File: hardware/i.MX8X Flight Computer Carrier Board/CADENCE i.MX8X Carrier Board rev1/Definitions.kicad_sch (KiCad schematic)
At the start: 12 parts, among them U43 TXS0101DCKR, U44 TXS0101DCKR, U45 TXS0101DCKR, U46 TXS0101DCKR, U47 TXS0108EPW

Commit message: peripheral & connector layout update
- finished rs-422 payload connector layout (changed footprint, package being used has around 40 left in stock at JLCPCB)
- modified memory (mram & nor flash) ic layouts & organized into layout blocks for easy placement later
- revised & reorganized gps, rtc, temp sensor, imu connections into separate layout  blocks. also moved around gps and moved peripherals into completed layout circuit block section for later placement
- changed some power monitor shunt resistor footprints so 10W or so doesnt go thru a sad 0402 resistor lol
- fixed microSD connection issues
- adjusted gps 50 ohm coax impedance connection (28 ohm trace + 22ohm resistor)
- 50 ohm impedance calculations for gps added to schematic & disclaimer for switching regulator low ripple burst mode added to power schematic page

to do:
- verify that board power monitor wont lead to reverse current driving i.mx8x and make it explode
- look further into & verify that cmos image sensor connector is correct one being used by lucid
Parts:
- renumbered R181 to R159, R182 to R160, R183 to R161, R184 to R162, R185 to R163
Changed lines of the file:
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@@
 		(on_board yes)
 		(dnp no)
-		(property "Reference" "R183"
+		(property "Reference" "R161"
 			(at 139.7 24.13 0)
 			(effects
@@
 			(project "CADENCE i.MX8X Carrier Board rev1"
 				(path "/de284495-d382-47cb-b528-76e440980d40/f5f49c98-aaea-4f03-a1b3-a277d1d06600/b523867a-62fb-4a81-ab53-06050067b1aa"
-					(reference "R183")
+					(reference "R161")
 					(unit 1)
 				)
@@
 		(on_board yes)
 		(dnp no)
-		(property "Reference" "R181"
+		(property "Reference" "R159"
 			(at 48.26 44.45 0)
 			(effects
@@
 			(project "CADENCE i.MX8X Carrier Board rev1"
 				(path "/de284495-d382-47cb-b528-76e440980d40/f5f49c98-aaea-4f03-a1b3-a277d1d06600/b523867a-62fb-4a81-ab53-06050067b1aa"
-					(reference "R181")
+					(reference "R159")
 					(unit 1)
 				)
@@
 		(on_board yes)
 		(dnp no)
-		(property "Reference" "R182"
+		(property "Reference" "R160"
 			(at 49.53 22.86 0)
 			(effects
@@
 			(project "CADENCE i.MX8X Carrier Board rev1"
 				(path "/de284495-d382-47cb-b528-76e440980d40/f5f49c98-aaea-4f03-a1b3-a277d1d06600/b523867a-62fb-4a81-ab53-06050067b1aa"
-					(reference "R182")
+					(reference "R160")
 					(unit 1)
 				)
@@
 		(dnp no)
 		(fields_autoplaced yes)
-		(property "Reference" "#FLG034"
+		(property "Reference" "#FLG032"
 			(at 209.55 24.765 0)
 			(effects
@@
 			(project "CADENCE i.MX8X Carrier Board rev1"
 				(path "/de284495-d382-47cb-b528-76e440980d40/f5f49c98-aaea-4f03-a1b3-a277d1d06600/b523867a-62fb-4a81-ab53-06050067b1aa"
-					(reference "#FLG034")
+					(reference "#FLG032")
 					(unit 1)
 				)
@@
 		(on_board yes)
 		(dnp no)
-		(property "Reference" "R185"
+		(property "Reference" "R163"
 			(at 222.25 26.67 0)
 			(effects
@@
 			(project "CADENCE i.MX8X Carrier Board rev1"
 				(path "/de284495-d382-47cb-b528-76e440980d40/f5f49c98-aaea-4f03-a1b3-a277d1d06600/b523867a-62fb-4a81-ab53-06050067b1aa"
-					(reference "R185")
+					(reference "R163")
 					(unit 1)
 				)
@@
 		(on_board yes)
 		(dnp no)
-		(property "Reference" "R184"
+		(property "Reference" "R162"
 			(at 139.7 45.72 0)
 			(effects
@@
 			(project "CADENCE i.MX8X Carrier Board rev1"
 				(path "/de284495-d382-47cb-b528-76e440980d40/f5f49c98-aaea-4f03-a1b3-a277d1d06600/b523867a-62fb-4a81-ab53-06050067b1aa"
-					(reference "R184")
+					(reference "R162")
 					(unit 1)
 				)
@@
 		(dnp no)
 		(fields_autoplaced yes)
-		(property "Reference" "#FLG033"
+		(property "Reference" "#FLG031"
 			(at 83.185 30.48 0)
 			(effects
@@
 			(project "CADENCE i.MX8X Carrier Board rev1"
 				(path "/de284495-d382-47cb-b528-76e440980d40/f5f49c98-aaea-4f03-a1b3-a277d1d06600/b523867a-62fb-4a81-ab53-06050067b1aa"
-					(reference "#FLG033")
-					(unit 1)
-				)
+					(reference "#FLG031")
+					(unit 1)
+				)

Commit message: layout update
- removed vbus regulators (left vbus unconnected for now, will reconnect to vbus on som later)
- outbound signal connectors to adcs & ebyte placement with i2c buffers and power monitors, etc
- layout block placement and some connections
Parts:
- renumbered C144 to C140, C145 to C141, U43 to U41, U44 to U42, U45 to U43, U46 to U44, U47 to U45
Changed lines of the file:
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@@
 		(on_board yes)
 		(dnp no)
-		(property "Reference" "#PWR0274"
+		(property "Reference" "#PWR0269"
 			(at 237.49 26.67 0)
 			(effects
@@
 			(project "CADENCE i.MX8X Carrier Board rev1"
 				(path "/de284495-d382-47cb-b528-76e440980d40/f5f49c98-aaea-4f03-a1b3-a277d1d06600/b523867a-62fb-4a81-ab53-06050067b1aa"
-					(reference "#PWR0274")
+					(reference "#PWR0269")
 					(unit 1)
 				)
@@
 		(on_board yes)
 		(dnp no)
-		(property "Reference" "#PWR0264"
+		(property "Reference" "#PWR0259"
 			(at 80.01 52.07 0)
 			(effects
@@
 			(project "CADENCE i.MX8X Carrier Board rev1"
 				(path "/de284495-d382-47cb-b528-76e440980d40/f5f49c98-aaea-4f03-a1b3-a277d1d06600/b523867a-62fb-4a81-ab53-06050067b1aa"
-					(reference "#PWR0264")
+					(reference "#PWR0259")
 					(unit 1)
 				)
@@
 		(on_board yes)
 		(dnp no)
-		(property "Reference" "#PWR0271"
+		(property "Reference" "#PWR0266"
 			(at 171.45 53.34 0)
 			(effects
@@
 			(project "CADENCE i.MX8X Carrier Board rev1"
 				(path "/de284495-d382-47cb-b528-76e440980d40/f5f49c98-aaea-4f03-a1b3-a277d1d06600/b523867a-62fb-4a81-ab53-06050067b1aa"
-					(reference "#PWR0271")
+					(reference "#PWR0266")
 					(unit 1)
 				)
@@
 		(on_board yes)
 		(dnp no)
-		(property "Reference" "U45"
+		(property "Reference" "U43"
 			(at 148.59 27.686 0)
 			(effects
@@
 			(project "CADENCE i.MX8X Carrier Board rev1"
 				(path "/de284495-d382-47cb-b528-76e440980d40/f5f49c98-aaea-4f03-a1b3-a277d1d06600/b523867a-62fb-4a81-ab53-06050067b1aa"
-					(reference "U45")
+					(reference "U43")
 					(unit 1)
 				)
@@
 		(on_board yes)
 		(dnp no)
-		(property "Reference" "C144"
+		(property "Reference" "C140"
 			(at 193.294 39.37 0)
 			(effects
@@
 			(project "CADENCE i.MX8X Carrier Board rev1"
 				(path "/de284495-d382-47cb-b528-76e440980d40/f5f49c98-aaea-4f03-a1b3-a277d1d06600/b523867a-62fb-4a81-ab53-06050067b1aa"
-					(reference "C144")
+					(reference "C140")
 					(unit 1)
 				)
@@
 		(on_board yes)
 		(dnp no)
-		(property "Reference" "U46"
+		(property "Reference" "U44"
 			(at 148.59 49.276 0)
 			(effects
@@
 			(project "CADENCE i.MX8X Carrier Board rev1"
 				(path "/de284495-d382-47cb-b528-76e440980d40/f5f49c98-aaea-4f03-a1b3-a277d1d06600/b523867a-62fb-4a81-ab53-06050067b1aa"
-					(reference "U46")
+					(reference "U44")
 					(unit 1)
 				)
@@
 		(on_board yes)
 		(dnp no)
-		(property "Reference" "#PWR0269"
+		(property "Reference" "#PWR0264"
 			(at 170.18 67.31 0)
 			(effects
@@
 			(project "CADENCE i.MX8X Carrier Board rev1"
 				(path "/de284495-d382-47cb-b528-76e440980d40/f5f49c98-aaea-4f03-a1b3-a277d1d06600/b523867a-62fb-4a81-ab53-06050067b1aa"
-					(reference "#PWR0269")
+					(reference "#PWR0264")
 					(unit 1)
 				)
@@
 		(on_board yes)
 		(dnp no)
-		(property "Reference" "#PWR0260"
+		(property "Reference" "#PWR0255"
 			(at 44.45 43.18 0)
 			(effects
@@
 			(project "CADENCE i.MX8X Carrier Board rev1"
 				(path "/de284495-d382-47cb-b528-76e440980d40/f5f49c98-aaea-4f03-a1b3-a277d1d06600/b523867a-62fb-4a81-ab53-06050067b1aa"
-					(reference "#PWR0260")
+					(reference "#PWR0255")
 					(unit 1)
 				)
@@
 		(on_board yes)
 		(dnp no)
-		(property "Reference" "#PWR0270"
+		(property "Reference" "#PWR0265"
 			(at 171.45 34.29 0)
 			(effects
@@
 			(project "CADENCE i.MX8X Carrier Board rev1"
 				(path "/de284495-d382-47cb-b528-76e440980d40/f5f49c98-aaea-4f03-a1b3-a277d1d06600/b523867a-62fb-4a81-ab53-06050067b1aa"
-					(reference "#PWR0270")
+					(reference "#PWR0265")
 					(unit 1)
 				)
@@
 		(on_board yes)
 		(dnp no)
-		(property "Reference" "C145"
+		(property "Reference" "C141"
 			(at 270.764 41.91 0)
 			(effects
@@
 			(project "CADENCE i.MX8X Carrier Board rev1"
 				(path "/de284495-d382-47cb-b528-76e440980d40/f5f49c98-aaea-4f03-a1b3-a277d1d06600/b523867a-62fb-4a81-ab53-06050067b1aa"
-					(reference "C145")
+					(reference "C141")
 					(unit 1)
 				)
@@
 		(on_board yes)
 		(dnp no)
-		(property "Reference" "#PWR0261"
+		(property "Reference" "#PWR0256"
 			(at 45.72 21.59 0)
 			(effects
@@
 			(project "CADENCE i.MX8X Carrier Board rev1"
 				(path "/de284495-d382-47cb-b528-76e440980d40/f5f49c98-aaea-4f03-a1b3-a277d1d06600/b523867a-62fb-4a81-ab53-06050067b1aa"
-					(reference "#PWR0261")
+					(reference "#PWR0256")
 					(unit 1)
 				)
@@
 		(on_board yes)
 		(dnp no)
-		(property "Reference" "#PWR0265"
+		(property "Reference" "#PWR0260"
 			(at 81.28 33.02 0)
 			(effects
@@
 			(project "CADENCE i.MX8X Carrier Board rev1"
 				(path "/de284495-d382-47cb-b528-76e440980d40/f5f49c98-aaea-4f03-a1b3-a277d1d06600/b523867a-62fb-4a81-ab53-06050067b1aa"
-					(reference "#PWR0265")
+					(reference "#PWR0260")
 					(unit 1)
 				)
@@
 		(on_board yes)
 		(dnp no)
-		(property "Reference" "#PWR0272"
+		(property "Reference" "#PWR0267"
 			(at 232.41 26.67 0)
 			(effects
@@
 			(project "CADENCE i.MX8X Carrier Board rev1"
 				(path "/de284495-d382-47cb-b528-76e440980d40/f5f49c98-aaea-4f03-a1b3-a277d1d06600/b523867a-62fb-4a81-ab53-06050067b1aa"
-					(reference "#PWR0272")
+					(reference "#PWR0267")
 					(unit 1)
 				)
@@
 		(on_board yes)
 		(dnp no)
-		(property "Reference" "U47"
+		(property "Reference" "U45"
 			(at 244.094 56.134 0)
 			(effects
@@
 			(project ""
 				(path "/de284495-d382-47cb-b528-76e440980d40/f5f49c98-aaea-4f03-a1b3-a277d1d06600/b523867a-62fb-4a81-ab53-06050067b1aa"
-					(reference "U47")
+					(reference "U45")
 					(unit 1)
 				)
@@
 		(on_board yes)
 		(dnp no)
-		(property "Reference" "#PWR0268"
+		(property "Reference" "#PWR0263"
 			(at 170.18 45.72 0)
 			(effects
@@
 			(project "CADENCE i.MX8X Carrier Board rev1"
 				(path "/de284495-d382-47cb-b528-76e440980d40/f5f49c98-aaea-4f03-a1b3-a277d1d06600/b523867a-62fb-4a81-ab53-06050067b1aa"
-					(reference "#PWR0268")
+					(reference "#PWR0263")
 					(unit 1)
 				)
@@
 		(dnp no)
 		(fields_autoplaced yes)
-		(property "Reference" "#FLG032"
+		(property "Reference" "#FLG030"
 			(at 209.55 24.765 0)
 			(effects
@@
 			(project "CADENCE i.MX8X Carrier Board rev1"
 				(path "/de284495-d382-47cb-b528-76e440980d40/f5f49c98-aaea-4f03-a1b3-a277d1d06600/b523867a-62fb-4a81-ab53-06050067b1aa"
-					(reference "#FLG032")
+					(reference "#FLG030")
 					(unit 1)
 				)
@@
 		(on_board yes)
 		(dnp no)
-		(property "Reference" "#PWR0267"
+		(property "Reference" "#PWR0262"
 			(at 135.89 44.45 0)
 			(effects
@@
 			(project "CADENCE i.MX8X Carrier Board rev1"
 				(path "/de284495-d382-47cb-b528-76e440980d40/f5f49c98-aaea-4f03-a1b3-a277d1d06600/b523867a-62fb-4a81-ab53-06050067b1aa"
-					(reference "#PWR0267")
+					(reference "#PWR0262")
 					(unit 1)
 				)
@@
 		(on_board yes)
 		(dnp no)
-		(property "Reference" "#PWR0262"
+		(property "Reference" "#PWR0257"
 			(at 78.74 66.04 0)
 			(effects
@@
 			(project "CADENCE i.MX8X Carrier Board rev1"
 				(path "/de284495-d382-47cb-b528-76e440980d40/f5f49c98-aaea-4f03-a1b3-a277d1d06600/b523867a-62fb-4a81-ab53-06050067b1aa"
-					(reference "#PWR0262")
+					(reference "#PWR0257")
 					(unit 1)
 				)
@@
 		(on_board yes)
 		(dnp no)
-		(property "Reference" "U44"
+		(property "Reference" "U42"
 			(at 58.42 26.416 0)
 			(effects
@@
 			(project "CADENCE i.MX8X Carrier Board rev1"
 				(path "/de284495-d382-47cb-b528-76e440980d40/f5f49c98-aaea-4f03-a1b3-a277d1d06600/b523867a-62fb-4a81-ab53-06050067b1aa"
-					(reference "U44")
+					(reference "U42")
 					(unit 1)
 				)
@@
 		(on_board yes)
 		(dnp no)
-		(property "Reference" "U43"
+		(property "Reference" "U41"
 			(at 57.15 48.006 0)
 			(effects
@@
 			(project "CADENCE i.MX8X Carrier Board rev1"
 				(path "/de284495-d382-47cb-b528-76e440980d40/f5f49c98-aaea-4f03-a1b3-a277d1d06600/b523867a-62fb-4a81-ab53-06050067b1aa"
-					(reference "U43")
+					(reference "U41")
 					(unit 1)
 				)
@@
 		(on_board yes)
 		(dnp no)
-		(property "Reference" "#PWR0266"
+		(property "Reference" "#PWR0261"
 			(at 135.89 24.13 0)
 			(effects
@@
 			(project "CADENCE i.MX8X Carrier Board rev1"
 				(path "/de284495-d382-47cb-b528-76e440980d40/f5f49c98-aaea-4f03-a1b3-a277d1d06600/b523867a-62fb-4a81-ab53-06050067b1aa"
-					(reference "#PWR0266")
+					(reference "#PWR0261")
 					(unit 1)
 				)
@@
 		(on_board yes)
 		(dnp no)
-		(property "Reference" "#PWR0263"
+		(property "Reference" "#PWR0258"
 			(at 80.01 44.45 0)
 			(effects
@@
 			(project "CADENCE i.MX8X Carrier Board rev1"
 				(path "/de284495-d382-47cb-b528-76e440980d40/f5f49c98-aaea-4f03-a1b3-a277d1d06600/b523867a-62fb-4a81-ab53-06050067b1aa"
-					(reference "#PWR0263")
+					(reference "#PWR0258")
 					(unit 1)
 				)
@@
 		(on_board yes)
 		(dnp no)
-		(property "Reference" "#PWR0273"
+		(property "Reference" "#PWR0268"
 			(at 234.95 68.58 0)
 			(effects
@@
 			(project "CADENCE i.MX8X Carrier Board rev1"
 				(path "/de284495-d382-47cb-b528-76e440980d40/f5f49c98-aaea-4f03-a1b3-a277d1d06600/b523867a-62fb-4a81-ab53-06050067b1aa"
-					(reference "#PWR0273")
+					(reference "#PWR0268")
 					(unit 1)
 				)
@@
 		(dnp no)
 		(fields_autoplaced yes)
-		(property "Reference" "#FLG031"
+		(property "Reference" "#FLG029"
 			(at 83.185 30.48 0)
 			(effects
@@
 			(project "CADENCE i.MX8X Carrier Board rev1"
 				(path "/de284495-d382-47cb-b528-76e440980d40/f5f49c98-aaea-4f03-a1b3-a277d1d06600/b523867a-62fb-4a81-ab53-06050067b1aa"
-					(reference "#FLG031")
-					(unit 1)
-				)
+					(reference "#FLG029")
+					(unit 1)
+				)

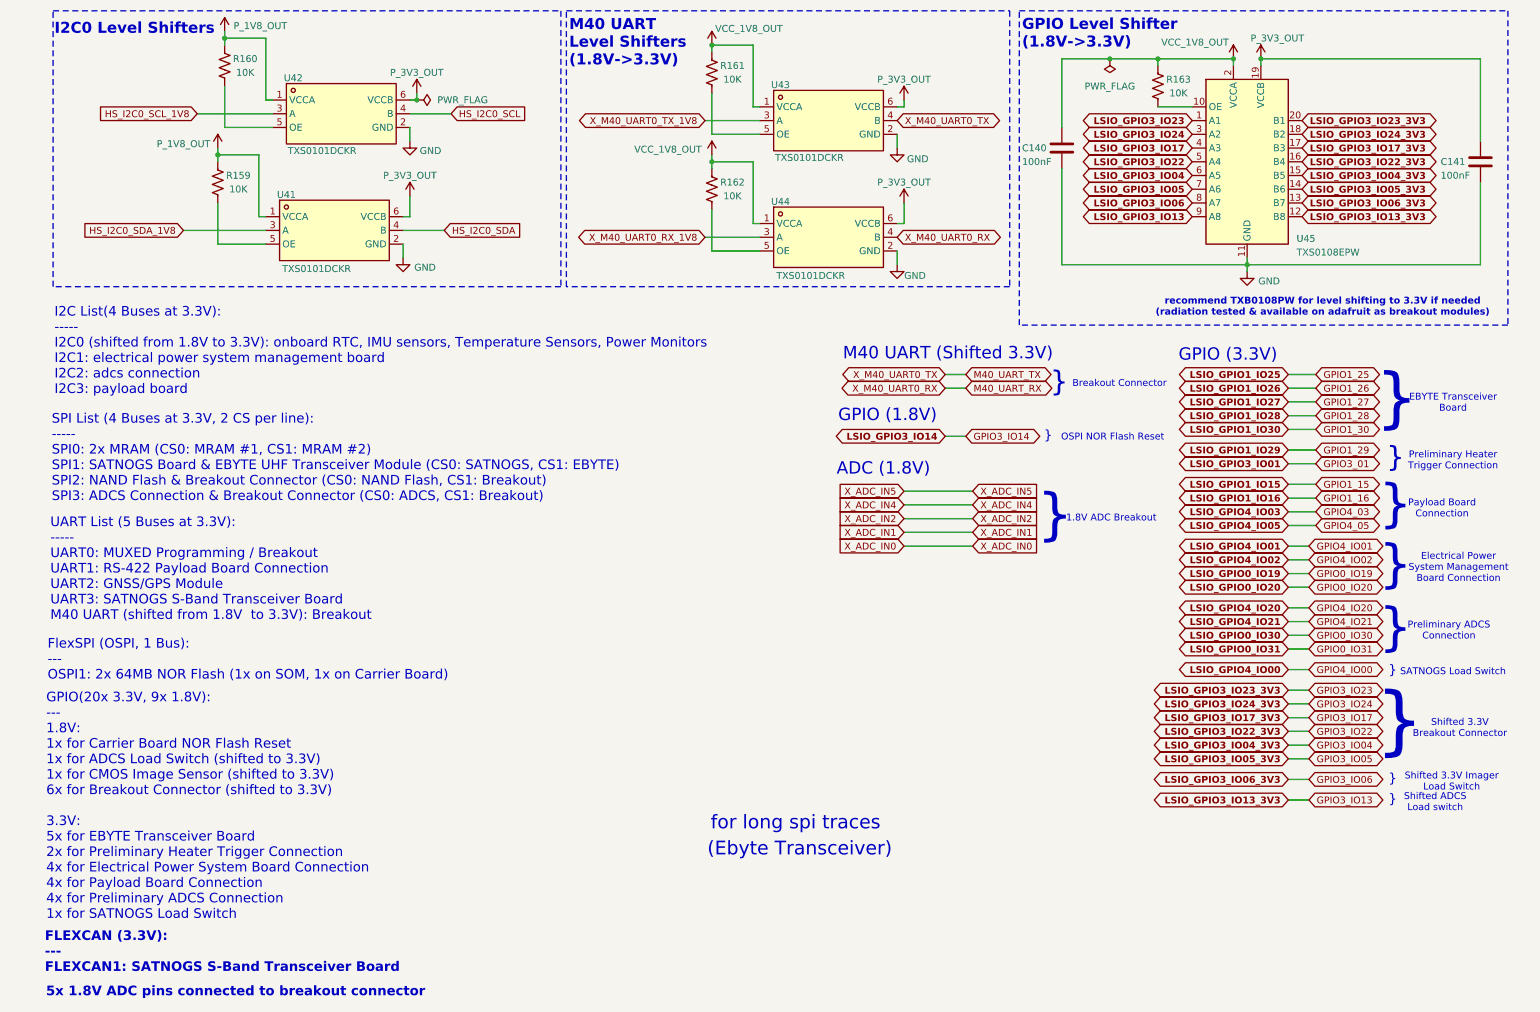
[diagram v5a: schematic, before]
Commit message: digital update
fixed microsd orientation, some digital connections disconnected from enet, removed some gnd and m40 uart header pins
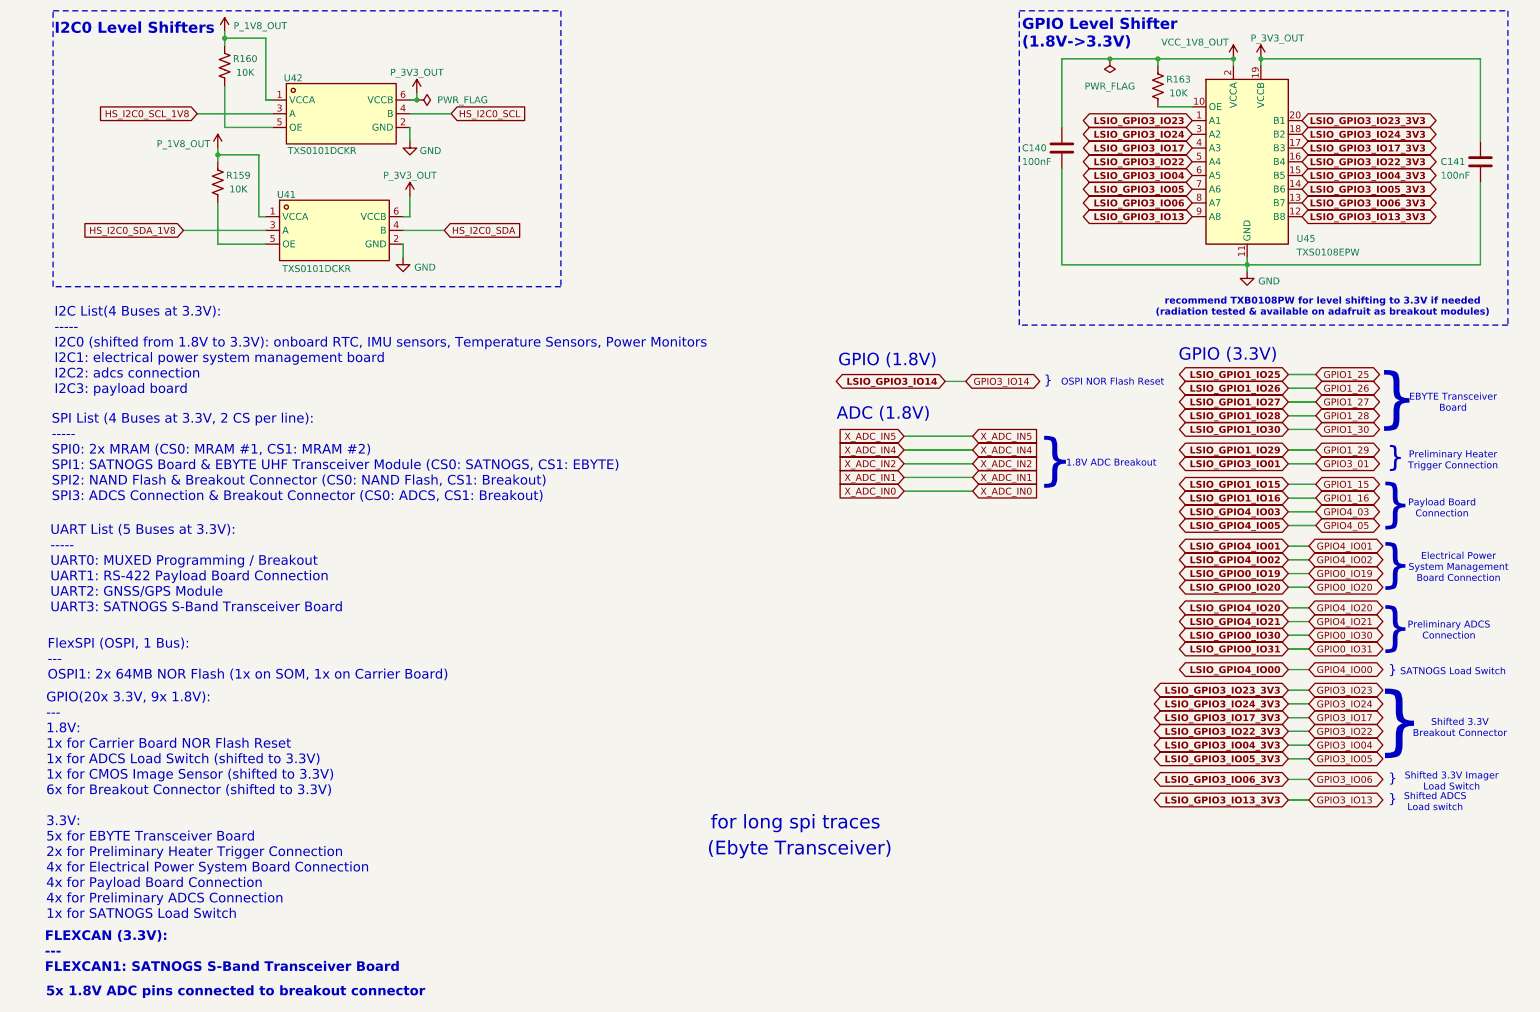
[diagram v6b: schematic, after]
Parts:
- removed R161, R162: 10K, Resistor_SMD:R_0402_1005Metric, symbol Device:R_US
- removed U43, U44: TXS0101DCKR, imx8_carrier_board_footprints:SC-70-6_L2.0-W1.3-P0.65-LS2.1-BR, symbol imx8_carrier_board_symbol_library:TXS0101DCKR
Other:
- note added: "UART List (5 Buses at 3.3V): ----- UART0: MUXED Programming / Breakout UART1: RS-422 Payload Board Connection UART2: GNSS/GPS Module UART3: SATNOGS S-Band Transceiver Board"
- note removed: "Breakout Connector"
- note removed: "M40 UART (Shifted 3.3V)"
- note removed: "M40 UART Level Shifters (1.8V->3.3V)"
- note removed: "UART List (5 Buses at 3.3V): ----- UART0: MUXED Programming / Breakout UART1: RS-422 Payload Board Connection UART2: GNSS/GPS Module UART3: SATNOGS S-Band Transceiver Board M40 UART (shifted from 1.8V to 3.3V): Breakout"
